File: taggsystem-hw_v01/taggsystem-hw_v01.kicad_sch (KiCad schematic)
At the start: 1 part, among them U1 ESP32-DevKitC-32E

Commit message: Add new comment
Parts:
- added L1: ~, taggsystem_library:L_1008_2520Metric, symbol taggsystem_library:IND_4U7_800mA_SMT_1008
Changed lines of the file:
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@@
 (kicad_sch (version 20230121) (generator eeschema)
   (paper "A4")
+  (symbol (lib_id "taggsystem_library:IND_4U7_800mA_SMT_1008") (at 217.17 73.66 0) (unit 1)
+    (in_bom yes) (on_board yes) (dnp no) (fields_autoplaced)
+    (property "Reference" "L1" (at 218.44 73.66 0)
+      (effects (font (size 1.27 1.27)) (justify left))
+    )
+    (property "Value" "~" (at 217.17 73.66 0)
+      (effects (font (size 1.27 1.27)))
+    )
+    (property "Footprint" "taggsystem_library:L_1008_2520Metric" (at 217.17 73.66 0)
+      (effects (font (size 1.27 1.27)) hide)
+    )
+    (property "Datasheet" "" (at 217.17 73.66 0)
+      (effects (font (size 1.27 1.27)) hide)
+    )
+    (pin "2")
+    (pin "1")
+    (instances
+      (project "taggsystem-hw_v01"
+        (path "/5001eb69-3e90-4730-a19d-343bf9eb5d0e"
+          (reference "L1") (unit 1)
+        )
+      )
+    )
+  )
   (symbol (lib_id "taggsystem_library:ESP32-DevKitC-32E") (at 147.32 107.95 0) (unit 1)
     (in_bom yes) (on_board yes) (dnp no) (fields_autoplaced)

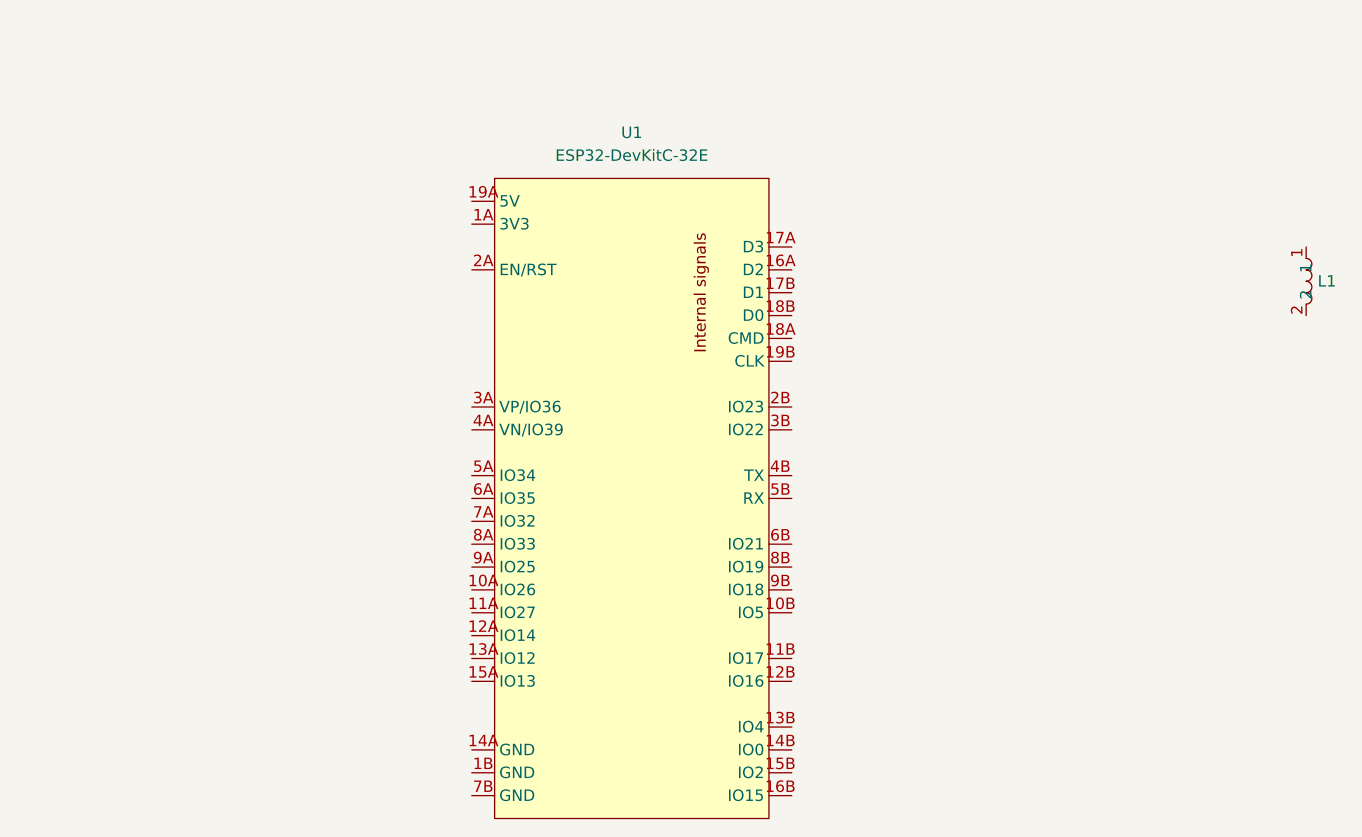
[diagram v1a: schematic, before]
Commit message: Add part number and manifacturer
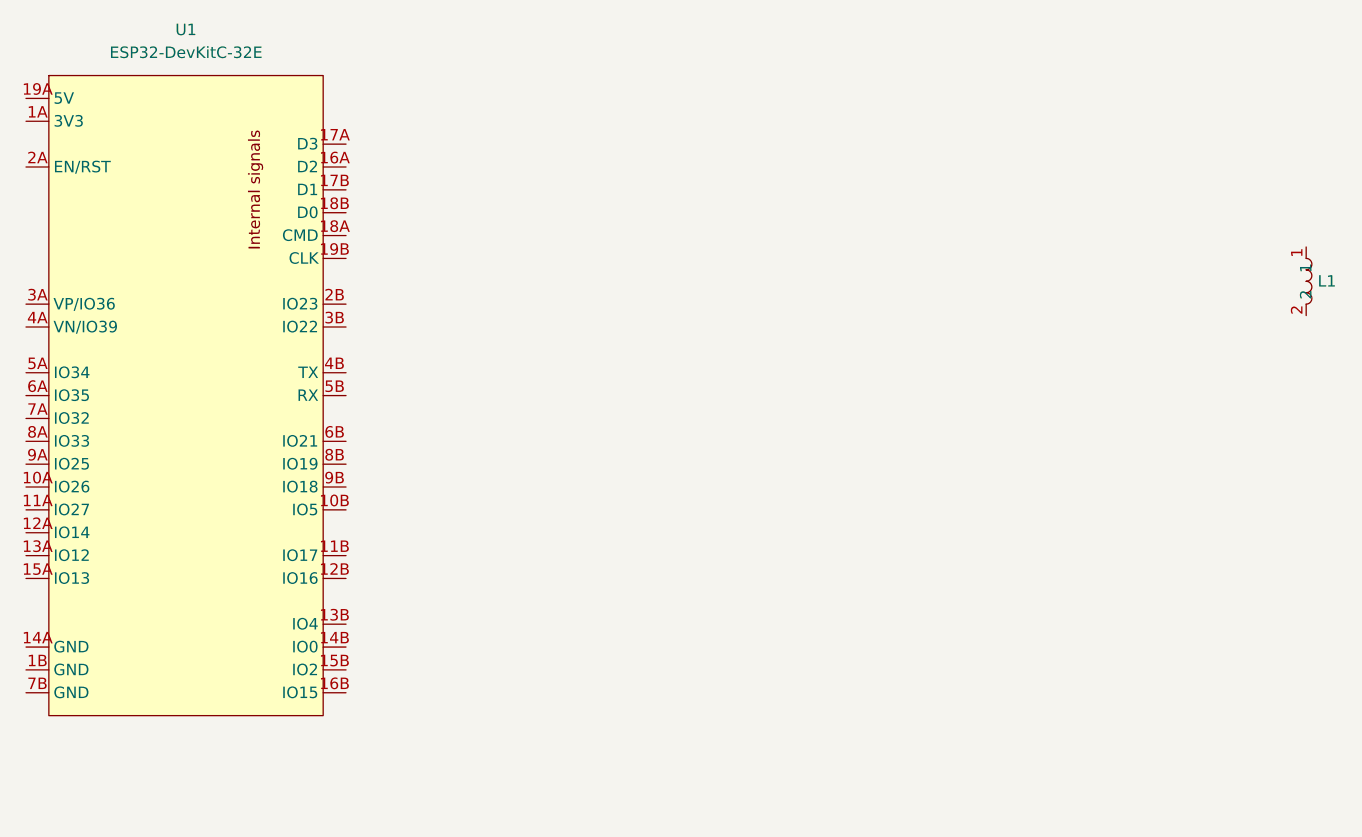
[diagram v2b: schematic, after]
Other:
- moved on the sheet: U1
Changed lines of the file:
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@@
     )
   )
-  (symbol (lib_id "taggsystem_library:ESP32-DevKitC-32E") (at 147.32 107.95 0) (unit 1)
+  (symbol (lib_id "taggsystem_library:ESP32-DevKitC-32E") (at 97.79 96.52 0) (unit 1)
     (in_bom yes) (on_board yes) (dnp no) (fields_autoplaced)
-    (property "Reference" "U1" (at 142.24 57.15 0)
+    (property "Reference" "U1" (at 92.71 45.72 0)
       (effects (font (size 1.27 1.27)))
     )
-    (property "Value" "ESP32-DevKitC-32E" (at 142.24 59.69 0)
+    (property "Value" "ESP32-DevKitC-32E" (at 92.71 48.26 0)
       (effects (font (size 1.27 1.27)))
     )
-    (property "Footprint" "taggsystem_library:ESP32-DEVKITC32E" (at 142.24 138.43 0)
+    (property "Footprint" "taggsystem_library:ESP32-DEVKITC32E" (at 92.71 127 0)
       (effects (font (size 1.27 1.27)) hide)
     )
-    (property "Datasheet" "https://docs.espressif.com/projects/esp-idf/en/latest/esp32/hw-reference/esp32/get-started-devkitc.html" (at 165.1 140.97 0)
+    (property "Datasheet" "https://docs.espressif.com/projects/esp-idf/en/latest/esp32/hw-reference/esp32/get-started-devkitc.html" (at 115.57 129.54 0)
       (effects (font (size 1.27 1.27)) hide)
     )

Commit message: Add to KiCad project
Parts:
- added U2: ~, 00_SOT:SOT23-6, symbol 00_IC_Power:IC_REG_BUCK_ADJ_17V_1A_SOT23
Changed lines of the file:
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@@
+    )
+  )
+  (symbol (lib_id "00_IC_Power:IC_REG_BUCK_ADJ_17V_1A_SOT23") (at 173.99 52.07 0) (unit 1)
+    (in_bom yes) (on_board yes) (dnp no) (fields_autoplaced)
+    (property "Reference" "U2" (at 182.88 53.34 0)
+      (effects (font (size 1.27 1.27)) (justify left))
+    )
+    (property "Value" "~" (at 171.45 52.07 0)
+      (effects (font (size 1.27 1.27)))
+    )
+    (property "Footprint" "00_SOT:SOT23-6" (at 173.99 69.85 0)
+      (effects (font (size 1.27 1.27)) hide)
+    )
+    (property "Datasheet" "https://www.ti.com/lit/ds/symlink/tps561201.pdf?HQS=dis-dk-null-digikeymode-dsf-pf-null-wwe&ts=1726943824021&ref_url=https%253A%252F%252Fwww.ti.com%252Fgeneral%252Fdocs%252Fsuppproductinfo.tsp%253FdistId%253D10%2526gotoUrl%253Dhttps%253A%252F%252Fwww.ti.com%252Flit%252Fgpn%252Ftps561201" (at 173.99 67.31 0)
+      (effects (font (size 1.27 1.27)) hide)
+    )
+    (property "Mfg1" "TI" (at 173.99 62.23 0)
+      (effects (font (size 1.27 1.27)) hide)
+    )
+    (property "Mfg1 pn" "TPS561201DDCR" (at 173.99 64.77 0)
+      (effects (font (size 1.27 1.27)) hide)
+    )
+    (pin "1")
+    (pin "3")
+    (pin "4")
+    (pin "5")
+    (pin "2")
+    (pin "6")
+    (instances
+      (project "taggsystem-hw_v01"
+        (path "/5001eb69-3e90-4730-a19d-343bf9eb5d0e"
+          (reference "U2") (unit 1)
+        )
+      )
     )
   )
